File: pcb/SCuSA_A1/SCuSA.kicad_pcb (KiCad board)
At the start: 2 copper layers, 51 x 42 mm, 79 parts, among them J101 USB4135-GF-A, J102 JST_S2B-PH-K-x, J103 Binding_Post_PKI_10_A_Au, J104 Binding_Post_PKI_10_A_Au, J105 SMA_Straight_Jack_Female, J107 77311-118-02LF, J108 77311-118-02LF, Q101 DMN2041LSD, SW101 JS202011CQN, SW102 JS202011CQN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

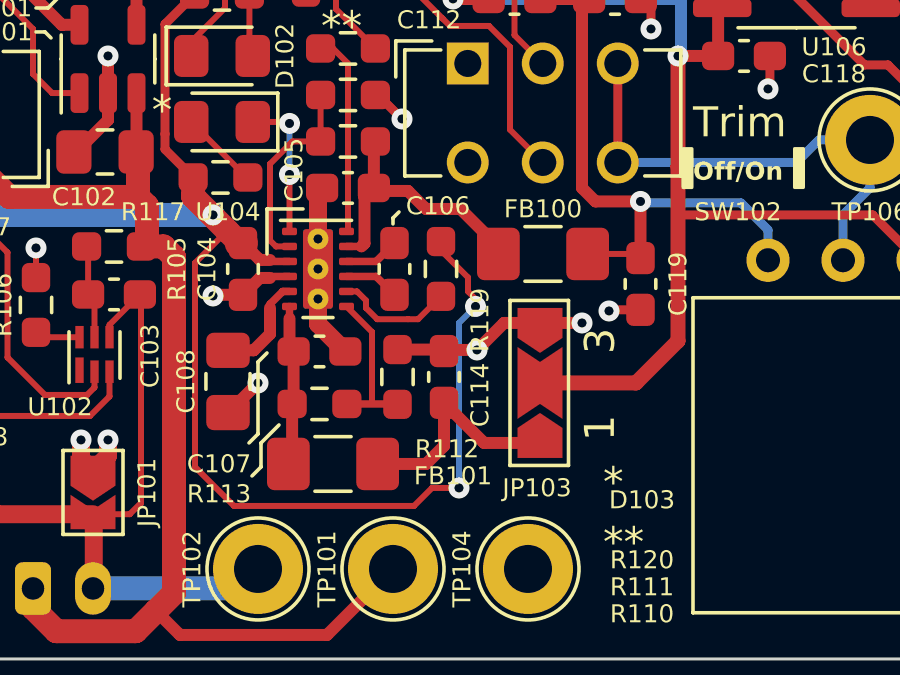
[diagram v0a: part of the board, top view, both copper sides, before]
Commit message: Increase charge current, change LED resistors
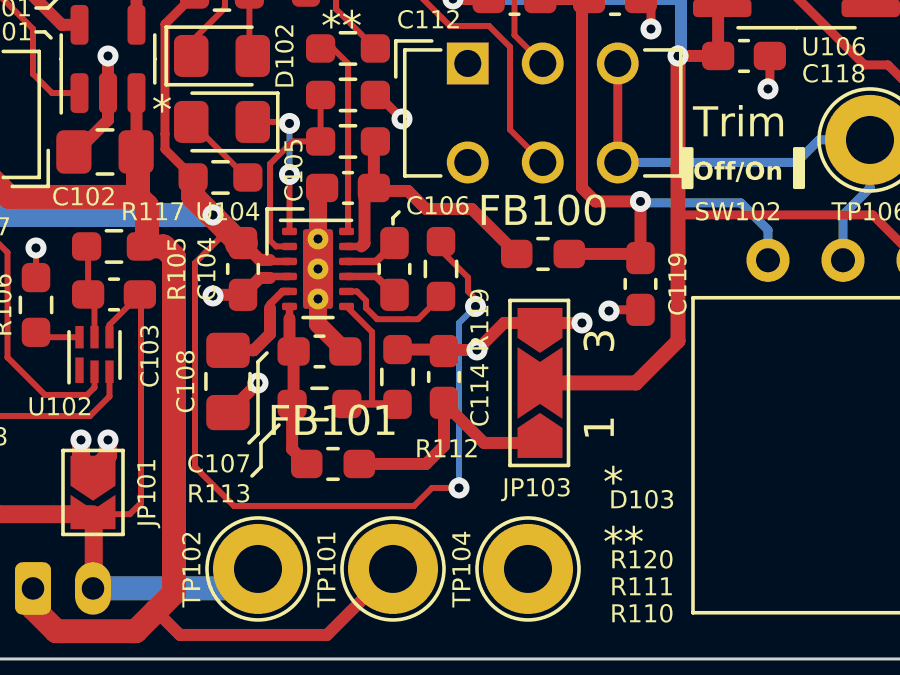
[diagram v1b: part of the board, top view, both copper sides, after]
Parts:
- C101, C102: value 1uF,16V,X7R,0603 -> 4.7uF,25V,X7R,0805
- FB100, FB101: footprint Inductor_SMD:L_1206_3216Metric_Pad1.42x1.75mm_HandSolder -> Inductor_SMD:L_0603_1608Metric_Pad1.05x0.95mm_HandSolder
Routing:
- net /-2V_filt: track 7.65 -> 8.27 mm
- net +3V3: track 38.8 -> 39.4 mm
